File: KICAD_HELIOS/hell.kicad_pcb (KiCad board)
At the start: 2 copper layers, 155 parts, among them J1 Conn_01x05, J3 NC3FAAH, J4 NC3MAAH, J5 ecran, SW1 SW_Push, SW2 SW_Push, U1 STM32F103C6Tx, U10 LM3404MA, U2 AMS1117-3.3, U3 MAX485E, U4 R-78B2.5-2.0, U5 LM3404MA, U6 LM3404MA, U7 LM3404MA, U8 LM3404MA, U9 LM3404MA

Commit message: organisation routage
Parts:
- removed J1: Conn_01x05, Connector_PinHeader_2.54mm:PinHeader_1x05_P2.54mm_Vertical
- removed SW2: SW_Push, Button_Switch_THT:SW_PUSH_6mm
- removed U4: R-78B2.5-2.0, Converter_DCDC:Converter_DCDC_RECOM_R-78B-2.0_THT
- added C24: 100n, Capacitor_SMD:C_0805_2012Metric, F.Cu at (44.0, 70.3)
- added C25: 10n, Capacitor_SMD:C_0805_2012Metric, F.Cu at (53.3, 38.6)
- added C26: 10n, Capacitor_SMD:C_0805_2012Metric, F.Cu at (38.3, 30.1)
- added J2: Conn_ST_STDC14, Connector_PinHeader_1.27mm:PinHeader_2x07_P1.27mm_Vertical_SMD, F.Cu at (35.2, 41.1)
- added R13: 10k, Resistor_SMD:R_1210_3225Metric, F.Cu at (52.7, 43.6)
- added R14: 10k, Resistor_SMD:R_1210_3225Metric, F.Cu at (38.3, 25.2)
- added R15: 10k, Resistor_SMD:R_1210_3225Metric, F.Cu at (42.3, 25.2)
- added R5: 1k, Resistor_SMD:R_1210_3225Metric, F.Cu at (58.0, 19.0)
- added R6: 10k, Resistor_SMD:R_1210_3225Metric, F.Cu at (52.8, 48.1)
- added SW3: SW_Push, Button_Switch_THT:SW_PUSH_6mm, F.Cu at (57.3, 33.6)
- added SW4: SW_Push, Button_Switch_THT:SW_PUSH_6mm, F.Cu at (34.8, 26.1)
- added U11: R-78B5.0-2.0, Converter_DCDC:Converter_DCDC_RECOM_R-78B-2.0_THT, F.Cu at (26.5, 61.8)
- C10: value 100u -> 1u
- C6, C7: value 100n -> 10u
- C9: value 10u -> 22u
- L1, L2: value 50u -> 68u
- L3, L4, L5, L6: value 50u -> 18u
- R1: value 10k -> 1k; footprint Resistor_SMD:R_0805_2012Metric -> Resistor_SMD:R_1210_3225Metric
- R3, R4: value 330 -> 1k6
- moved R11 265.4 mm to (79.5, 18.2), turned to -90 degrees
- moved R7 254.9 mm to (79.0, 36.6), turned to -90 degrees
- moved R9 251.5 mm to (78.5, 52.2), turned to -90 degrees
- moved C11 247.0 mm to (86.0, 13.0)
- moved C22 244.8 mm to (93.0, 18.9), turned to 90 degrees
- moved C23 244.6 mm to (79.5, 78.0), turned to -90 degrees
- moved L2 244.5 mm to (81.4, 73.5), turned to 180 degrees
- moved L1 243.3 mm to (90.6, 24.0)
- moved L4 242.2 mm to (80.9, 88.0), turned to 180 degrees
- moved C14 241.0 mm to (86.6, 29.9)
- moved L6 240.5 mm to (79.9, 104.0), turned to 180 degrees
- moved C21 239.8 mm to (79.0, 92.5), turned to -90 degrees
- moved U5 239.6 mm to (86.5, 17.5), turned to 180 degrees
- moved R12 238.5 mm to (94.0, 78.8), turned to 90 degrees
- moved L3 238.4 mm to (91.1, 40.4)
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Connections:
- C12 pad 1: Net-(C12-Pad1) -> GND
- C7 pad 1: GND -> +5V
- C7 pad 2: +5V -> GND
- R1 pad 1: +3.3V -> Ecr_SCL
- R1 pad 2: Net-(C12-Pad1) -> +3.3V
- SW1 pad 1: BOUTTON_1 -> Net-(R13-Pad2)
- SW1 pad 2: +3.3V -> GND
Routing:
- net Net-(D69-Pad3): track 9.86 -> 0.00 mm
- net Net-(D69-Pad5): track 9.27 -> 0.00 mm
- net Net-(D69-Pad1): track 9.27 -> 0.00 mm
- net (no net): track 3.82 -> 0.00 mm
- net DMX_N: track 1.44 -> 0.00 mm

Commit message: PCB Routage 1ver
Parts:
- moved J3 61.5 mm to (63.0, 134.6)
- moved J4 53.3 mm to (83.1, 119.9)
- moved R11 48.4 mm to (119.7, 45.0), turned to 90 degrees
- moved R9 47.5 mm to (120.8, 73.7), turned to 90 degrees
- moved R7 47.3 mm to (120.7, 58.9), turned to 90 degrees
- moved SW4 47.0 mm to (65.2, 61.9)
- moved C24 46.7 mm to (70.7, 108.5)
- moved C11 46.0 mm to (113.2, 50.2), turned to 180 degrees
- moved R6 45.4 mm to (86.6, 78.4)
- moved D1 45.1 mm to (83.1, 51.5)
- moved D2 45.1 mm to (79.1, 51.5)
- moved R14 45.1 mm to (71.1, 56.0)
- moved R15 45.1 mm to (75.1, 56.0)
- moved R3 45.1 mm to (83.1, 56.0)
- moved R4 45.1 mm to (79.1, 56.0)
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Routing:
- net GND: track 0.00 -> 171.8 mm, vias 0 -> 6
- net LEDB2: track 0.00 -> 119.3 mm
- net /Driver_49LED_RGB_2/G_49_Anode: track 0.00 -> 93.5 mm
- net DMX_N: track 0.00 -> 92.6 mm
- net +3.3V: track 0.00 -> 92.2 mm
- net /Driver_49LED_RGB_1/R_49_Anode: track 0.00 -> 89.1 mm
- net /Driver_49LED_RGB_1/B_49_Anode: track 0.00 -> 87.5 mm, vias 0 -> 16
- net DMX_P: track 0.00 -> 85.5 mm
- net /Driver_49LED_RGB_2/R_49_Anode: track 0.00 -> 85.2 mm
- net /Driver_49LED_RGB_2/B_49_Anode: track 0.00 -> 81.9 mm, vias 0 -> 14
- net /Driver_49LED_RGB_1/G_49_Anode: track 0.00 -> 81.0 mm
- net +24V: track 0.00 -> 80.2 mm
- net LEDG2: track 0.00 -> 77.2 mm
- net Ecr_SCL: track 0.00 -> 74.8 mm
- net Ecr_SDA: track 0.00 -> 64.7 mm, vias 0 -> 6
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- added copper zone on B.Cu, net GND
- added copper zone on F.Cu, net GND

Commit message: update pcb
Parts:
- added H101: MountingHole_Pad, MountingHole:MountingHole_3.2mm_M3_DIN965_Pad, F.Cu at (90.0, 40.0)
- added H102: MountingHole_Pad, MountingHole:MountingHole_3.2mm_M3_DIN965_Pad, F.Cu at (90.0, 118.0)
- added H103: MountingHole_Pad, MountingHole:MountingHole_3.2mm_M3_DIN965_Pad, F.Cu at (126.0, 40.0)
- added H104: MountingHole_Pad, MountingHole:MountingHole_3.2mm_M3_DIN965_Pad, F.Cu at (126.0, 118.0)
- added H105: MountingHole_Pad, MountingHole:MountingHole_3.2mm_M3_DIN965_Pad, F.Cu at (191.0, 40.0)
- added H106: MountingHole_Pad, MountingHole:MountingHole_3.2mm_M3_DIN965_Pad, F.Cu at (191.0, 118.0)
- added J105: Conn_01x02, Connector_AMASS:AMASS_XT30U-M_1x02_P5.0mm_Vertical, F.Cu at (114.0, 40.0)
- moved C113 77.1 mm to (-5.95, 59.6)
- moved C114 77.1 mm to (9.05, 67.2)
- moved R107 77.1 mm to (2.91, 71.6)
- moved C106 77.1 mm to (-16.0, 67.1)
- moved C107 77.1 mm to (-16.0, 70.1)
- moved C108 77.1 mm to (-16.0, 79.1)
- moved C109 77.1 mm to (-16.0, 76.1)
- moved C110 77.1 mm to (-16.0, 73.1)
- moved C111 77.1 mm to (19.2, 44.0)
- moved C112 77.1 mm to (24.2, 61.8)
- moved D101 77.1 mm to (6.00, 50.9)
- moved D102 77.1 mm to (2.00, 50.9)
- moved J103 77.1 mm to (-25.5, 39.5)
- moved J104 77.1 mm to (-9.05, 70.6)
- moved R101 77.1 mm to (-2.00, 55.4)
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- renumbered C6 to C101, C7 to C102, C8 to C103, C9 to C104, C24 to C105, C5 to C106, C4 to C107, C1 to C108, C2 to C109, C3 to C110, C23 to C1101, C13 to C1102, C21 to C1103, C15 to C1104, C19 to C1105, C17 to C1106, C10 to C111, C12 to C112, C26 to C113, C25 to C114, C22 to C201, C11 to C202, C20 to C203, C14 to C204, C18 to C205, C16 to C206, D93 to D1001, D9 to D1002, D23 to D1003, D37 to D1004, D51 to D1005, D65 to D1006, D79 to D1007, D1 to D101, D2 to D102, D94 to D1301, D10 to D1302, D24 to D1303, D38 to D1304, D52 to D1305, D66 to D1306, D80 to D1307, D95 to D1401, D11 to D1402, D25 to D1403, D39 to D1404, D53 to D1405, D67 to D1406, D81 to D1407, D96 to D1501, D12 to D1502, D26 to D1503, D40 to D1504, D54 to D1505, D68 to D1506, D82 to D1507, D97 to D1601, D13 to D1602, D27 to D1603, D41 to D1604, D55 to D1605, D69 to D1606, D83 to D1607, D98 to D1701, D14 to D1702, D28 to D1703, D42 to D1704, D56 to D1705, D70 to D1706, D84 to D1707, D99 to D1801, D15 to D1802, D29 to D1803, D43 to D1804, D57 to D1805, D71 to D1806, D85 to D1807, D100 to D1901, D16 to D1902, D30 to D1903, D44 to D1904, D58 to D1905, D72 to D1906, D86 to D1907, D87 to D401, D3 to D402, D17 to D403, D31 to D404, D45 to D405, D59 to D406, D73 to D407, D88 to D501, D4 to D502, D18 to D503, D32 to D504, D46 to D505, D60 to D506, D74 to D507, D89 to D601, D5 to D602, D19 to D603, D33 to D604, D47 to D605, D61 to D606, D75 to D607, D90 to D701, D6 to D702, D20 to D703, D34 to D704, D48 to D705, D62 to D706, D76 to D707, D91 to D801, D7 to D802, D21 to D803, D35 to D804, D49 to D805, D63 to D806, D77 to D807, D92 to D901, D8 to D902, D22 to D903, D36 to D904, D50 to D905, D64 to D906, D78 to D907, J3 to J101, J4 to J102, J5 to J103, J2 to J104, L2 to L1101, L4 to L1102, L6 to L1103, L1 to L201, L3 to L202, L5 to L203, R15 to R101, R1 to R102, R5 to R103, R6 to R104, R14 to R105, R13 to R106, R2 to R107, R3 to R108, R4 to R109, R12 to R1101, R8 to R1102, R10 to R1103, R11 to R201, R7 to R202, R9 to R203, SW3 to SW101, SW4 to SW102, SW1 to SW103, U11 to U101, U2 to U102, U3 to U103, U1 to U104, U8 to U1101, U9 to U1102, U10 to U1103, U5 to U201, U6 to U202, U7 to U203
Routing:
- net LEDB2: track 119.3 -> 0.00 mm
- net DMX_N: track 92.6 -> 0.00 mm
- net +3.3V: track 92.2 -> 0.00 mm
- net GND: track 171.8 -> 79.8 mm, vias 6 -> 42
- net DMX_P: track 85.5 -> 0.00 mm
- net +24V: track 80.2 -> 0.00 mm
- net /Driver_49LED_RGB_2/G_49_Anode: track 93.5 -> 14.7 mm, vias 0 -> 7
- net LEDG2: track 77.2 -> 0.00 mm
- net Ecr_SCL: track 74.8 -> 0.00 mm
- net /Driver_49LED_RGB_1/R_49_Anode: track 89.1 -> 14.7 mm, vias 0 -> 7
- net /Driver_49LED_RGB_1/B_49_Anode: track 87.5 -> 14.7 mm, vias 16 -> 7
- net /Driver_49LED_RGB_2/R_49_Anode: track 85.2 -> 14.7 mm, vias 0 -> 7
- net /Driver_49LED_RGB_2/B_49_Anode: track 81.9 -> 14.7 mm, vias 14 -> 7
- net /Driver_49LED_RGB_1/G_49_Anode: track 81.0 -> 14.7 mm, vias 0 -> 7
- net Ecr_SDA: track 64.7 -> 0.00 mm, vias 6 -> 0
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- added copper zone on In2.Cu, net +24V
- added copper zone on In2.Cu, net +3.3V
- added copper zone on In2.Cu, net +5V
- added copper zone on In2.Cu, net /Driver_49LED_RGB_1/B_49_Anode
- added copper zone on B.Cu, net /Driver_49LED_RGB_1/G_49_Anode
- added copper zone on F.Cu, net /Driver_49LED_RGB_1/R_49_Anode
- added copper zone on In2.Cu, net /Driver_49LED_RGB_2/B_49_Anode
- added copper zone on B.Cu, net /Driver_49LED_RGB_2/G_49_Anode
- added copper zone on F.Cu, net /Driver_49LED_RGB_2/R_49_Anode
- added copper zone on In1.Cu, net GND
- added copper zone on In2.Cu, net GND
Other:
- board outline added: 109 x 86 mm
- copper layers 2 -> 4

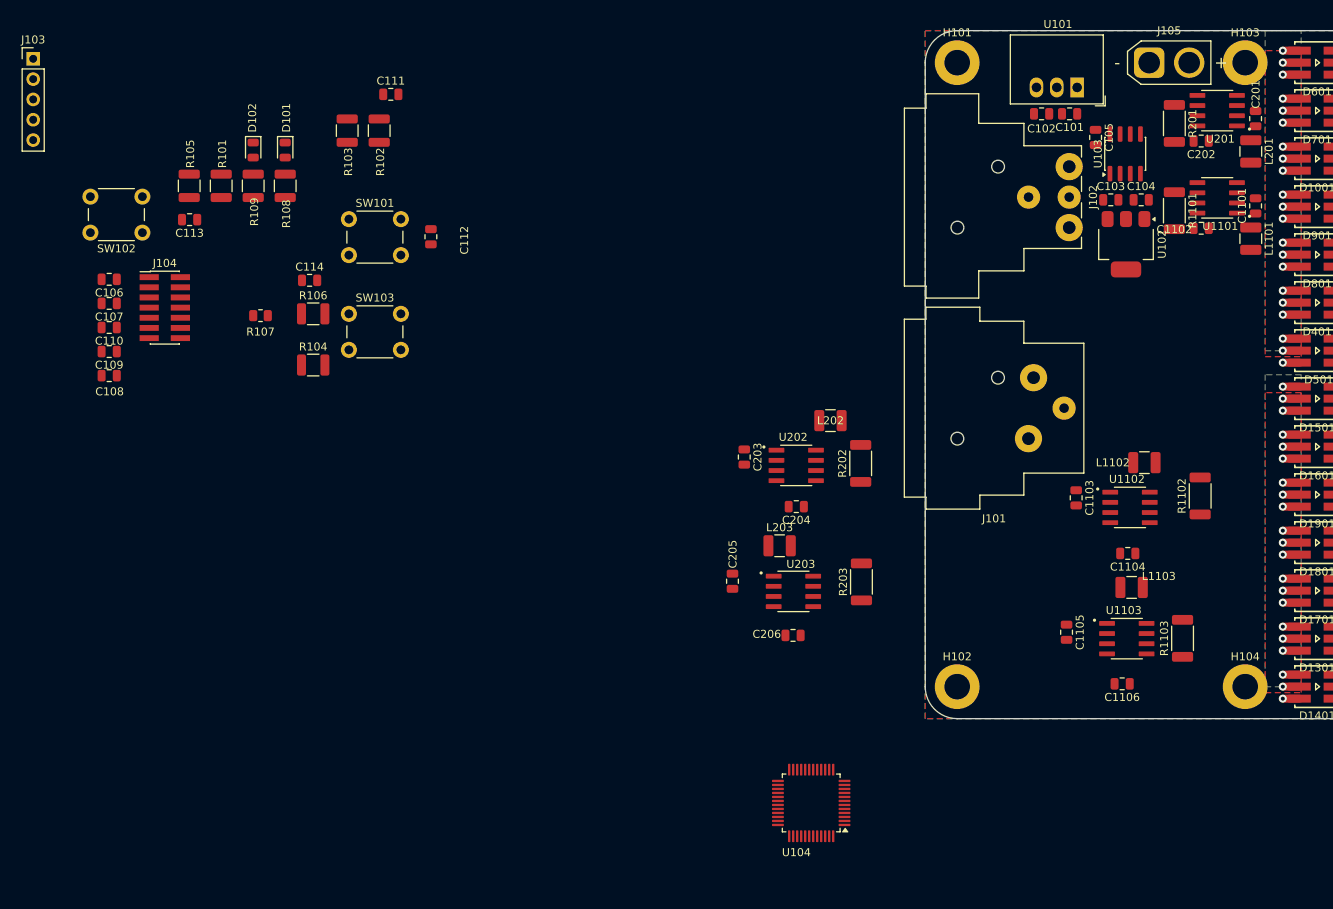
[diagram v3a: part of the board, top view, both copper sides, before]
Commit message: Kicad PCB et changement de quelques empreintes
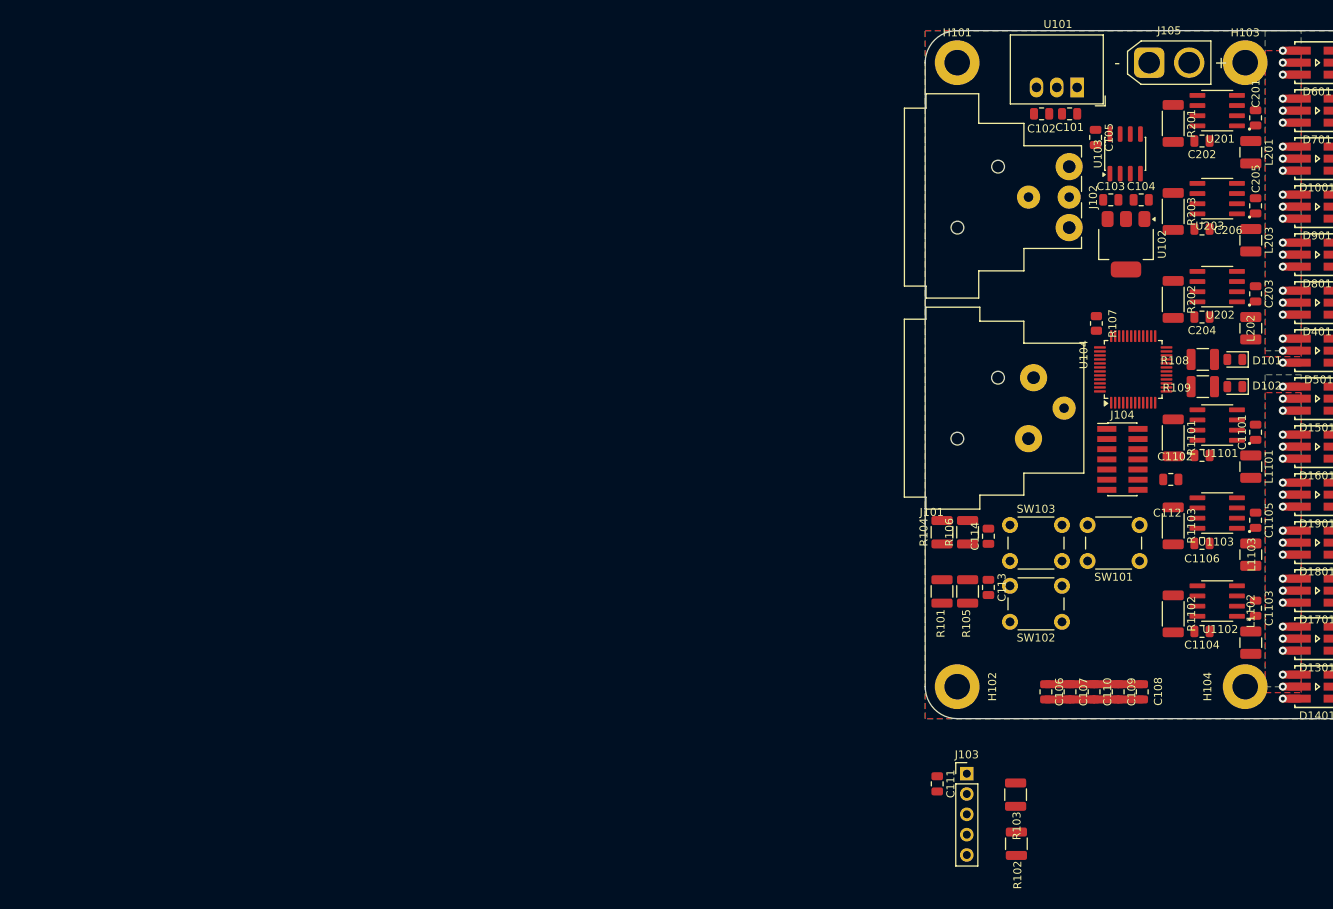
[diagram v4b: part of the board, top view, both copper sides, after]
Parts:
- moved J103 147.0 mm to (91.2, 128.9)
- moved C108 135.0 mm to (113.1, 118.7), turned to -90 degrees
- moved C109 133.1 mm to (110.1, 118.7), turned to -90 degrees
- moved C110 131.3 mm to (107.1, 118.7), turned to -90 degrees
- moved C107 129.5 mm to (104.1, 118.7), turned to -90 degrees
- moved C106 127.9 mm to (101.1, 118.7), turned to -90 degrees
- moved D102 126.2 mm to (124.7, 80.5), turned to 180 degrees
- moved SW102 124.8 mm to (103.1, 109.9)
- moved D101 121.6 mm to (124.7, 77.1), turned to 180 degrees
- moved R109 121.3 mm to (120.7, 80.5), turned to 0 degrees
- moved J104 121.2 mm to (110.7, 89.6)
- moved R102 119.5 mm to (97.4, 137.6)
- moved R103 117.8 mm to (97.3, 131.5)
- moved R108 116.7 mm to (120.7, 77.1), turned to 0 degrees
- moved C111 110.0 mm to (87.5, 130.2), turned to -90 degrees
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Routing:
- net GND: track 79.8 -> 91.8 mm
- net +3.3V: track 0.00 -> 12.0 mm

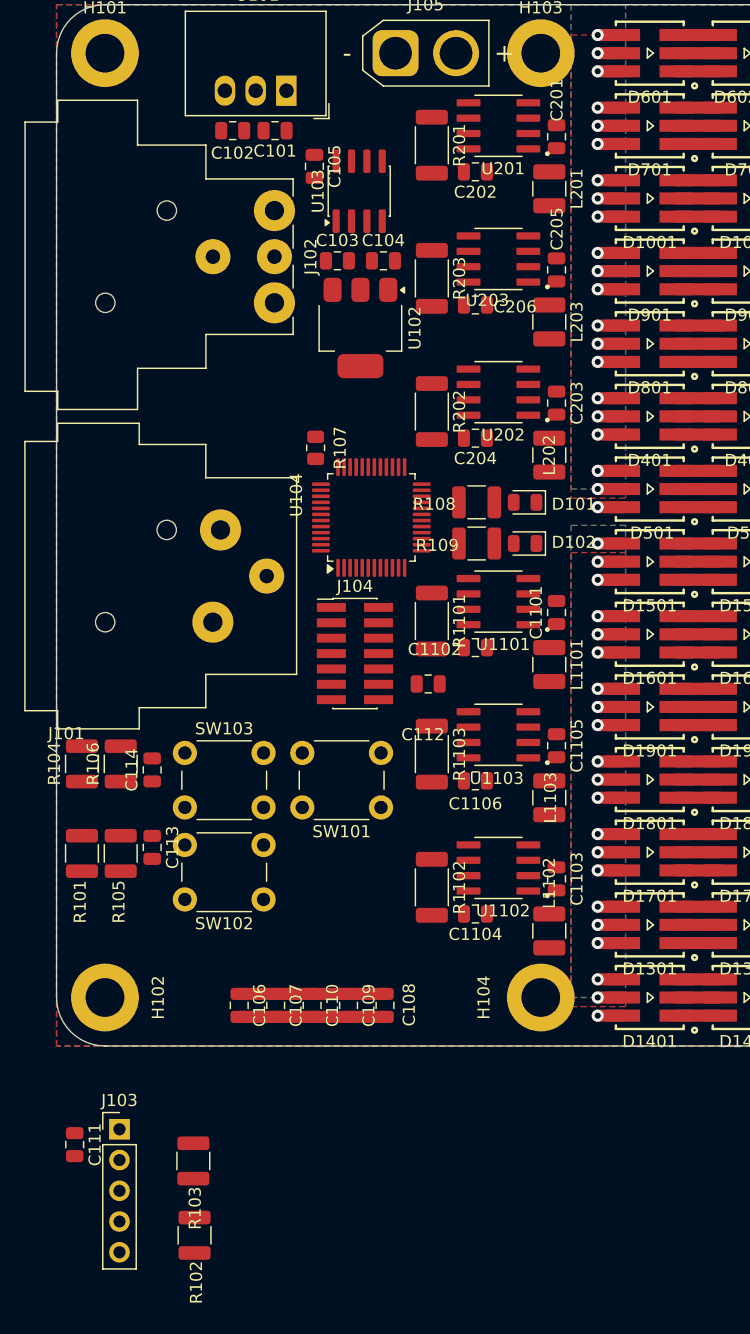
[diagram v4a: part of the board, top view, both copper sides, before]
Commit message: Routage presque fini en attente de modification d'empreinte
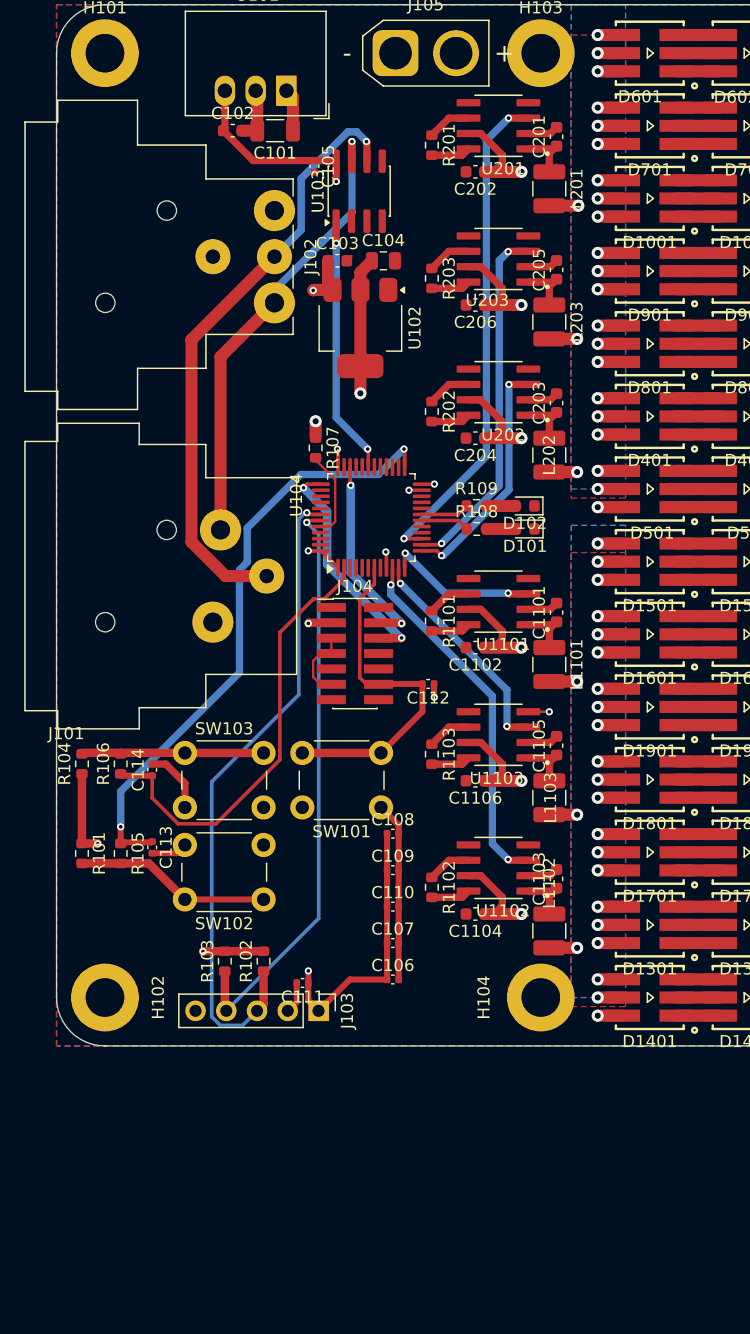
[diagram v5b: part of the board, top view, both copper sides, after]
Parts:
- C101: footprint Capacitor_SMD:C_0805_2012Metric -> Capacitor_SMD:C_1206_3216Metric
- C102, C103, C1101, C1102, C1103, C1104, C1105, C1106, C201, C202, C203, C204, C205, C206: footprint Capacitor_SMD:C_0805_2012Metric -> Capacitor_SMD:C_0603_1608Metric
- C105, C106, C107, C108, C109, C110, C111, C112, C113, C114: footprint Capacitor_SMD:C_0805_2012Metric -> Capacitor_SMD:C_0402_1005Metric
- D101, D102: footprint LED_SMD:LED_0805_2012Metric -> LED_SMD:LED_0603_1608Metric
- L1101, L201: value 68u -> 18u
- R101, R102, R103, R104, R105, R106, R108, R109: footprint Resistor_SMD:R_1210_3225Metric -> Resistor_SMD:R_0603_1608Metric
- R107: footprint Resistor_SMD:R_0805_2012Metric -> Resistor_SMD:R_0603_1608Metric
- R1101, R1102, R1103, R201, R202, R203: footprint Resistor_SMD:R_2010_5025Metric -> Resistor_SMD:R_0603_1608Metric
- moved R102 23.3 mm to (103.1, 115.0)
- moved C111 23.1 mm to (106.3, 116.8), turned to 180 degrees
- moved J103 19.1 mm to (107.6, 119.1), turned to -90 degrees
- moved R103 16.7 mm to (99.9, 115.0)
- moved C108 14.2 mm to (113.8, 104.5), turned to 0 degrees
- moved C106 12.9 mm to (113.8, 116.5), turned to 0 degrees
- moved C109 11.8 mm to (113.8, 107.5), turned to 0 degrees
- moved C107 11.0 mm to (113.8, 113.5), turned to 0 degrees
- moved C110 10.5 mm to (113.8, 110.5), turned to 0 degrees
- moved D102 3.10 mm to (124.7, 77.4)
- moved R109 3.10 mm to (120.7, 77.4)
- moved D101 2.20 mm to (124.7, 79.3)
- moved R108 2.20 mm to (120.7, 79.3)
- turned C1103 to 90 degrees
- turned C1105 to 90 degrees
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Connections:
- U104 pad 10: LEDR1 -> LEDG2
- U104 pad 11: LEDG1 -> LEDB2
- U104 pad 12: LEDB1 -> LEDR2
- U104 pad 13: LEDR2 -> LEDG1
- U104 pad 14: LEDG2 -> LEDB1
- U104 pad 15: LEDB2 -> LEDR1
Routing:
- net +24V: track 0.00 -> 145.9 mm, vias 0 -> 6
- net GND: track 91.8 -> 157.1 mm, vias 42 -> 46
- net Ecr_SCL: track 0.00 -> 54.2 mm, vias 0 -> 1
- net DMX_P: track 0.00 -> 50.1 mm, vias 0 -> 1
- net BOUTTON_2: track 0.00 -> 50.1 mm, vias 0 -> 2
- net Ecr_SDA: track 0.00 -> 48.5 mm, vias 0 -> 1
- net +3.3V: track 12.0 -> 54.7 mm, vias 0 -> 9
- net LEDR1: track 0.00 -> 41.5 mm, vias 0 -> 2
- net DMX_N: track 0.00 -> 38.2 mm, vias 0 -> 1
- net BOUTTON_1: track 0.00 -> 36.7 mm
- net LEDG2: track 0.00 -> 29.9 mm, vias 0 -> 2
- net LEDB1: track 0.00 -> 29.7 mm, vias 0 -> 2
- net NRST: track 0.00 -> 28.6 mm
- net DMX_RX: track 0.00 -> 21.4 mm, vias 0 -> 2
- net LEDG1: track 0.00 -> 19.9 mm, vias 0 -> 2
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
